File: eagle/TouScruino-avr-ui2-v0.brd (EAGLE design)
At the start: 63.5 x 72.4 mm, 60 parts, among them J1 AVR_ISP, Q1 8MHz, Q2 MMBT2222A, Q3 8MHz, U1 ATMEGA1284P, U2 AR1021, U3 MIC5209-3.3YS, U4 MCP73831, X2 USB

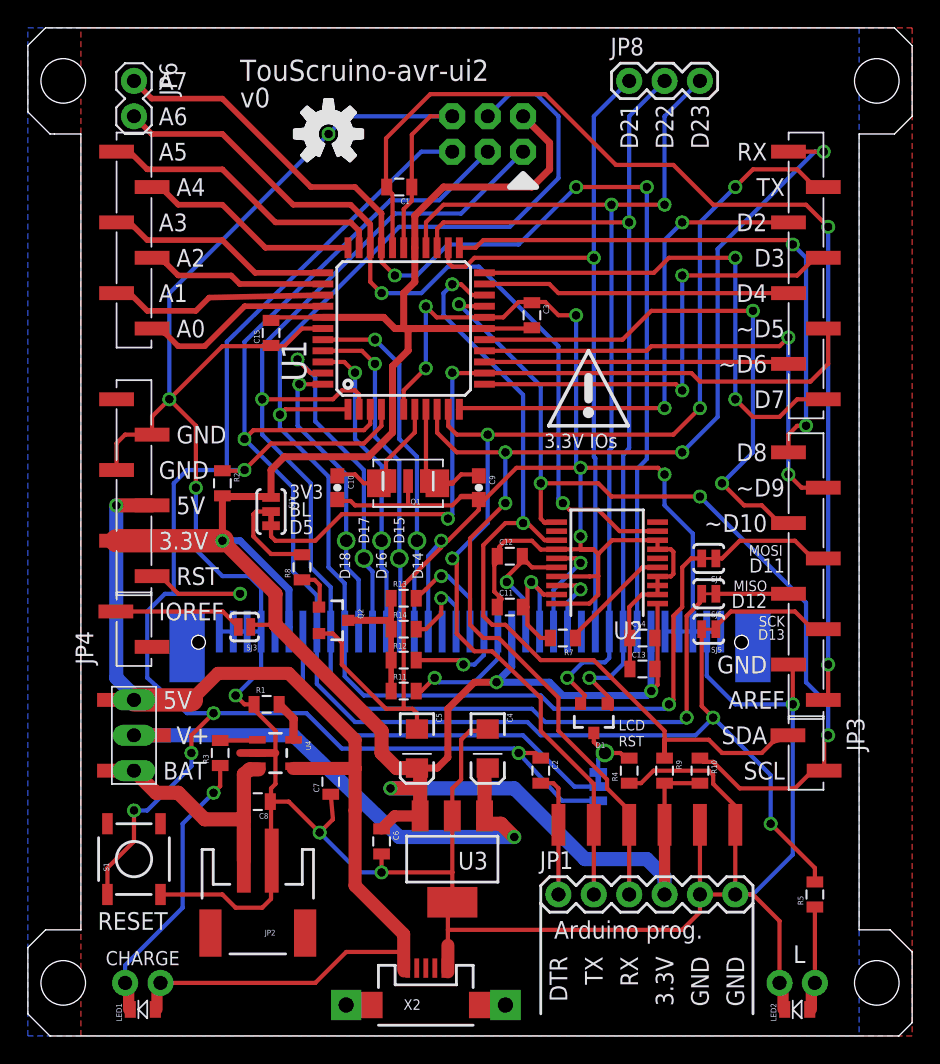
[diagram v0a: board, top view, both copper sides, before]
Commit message: 
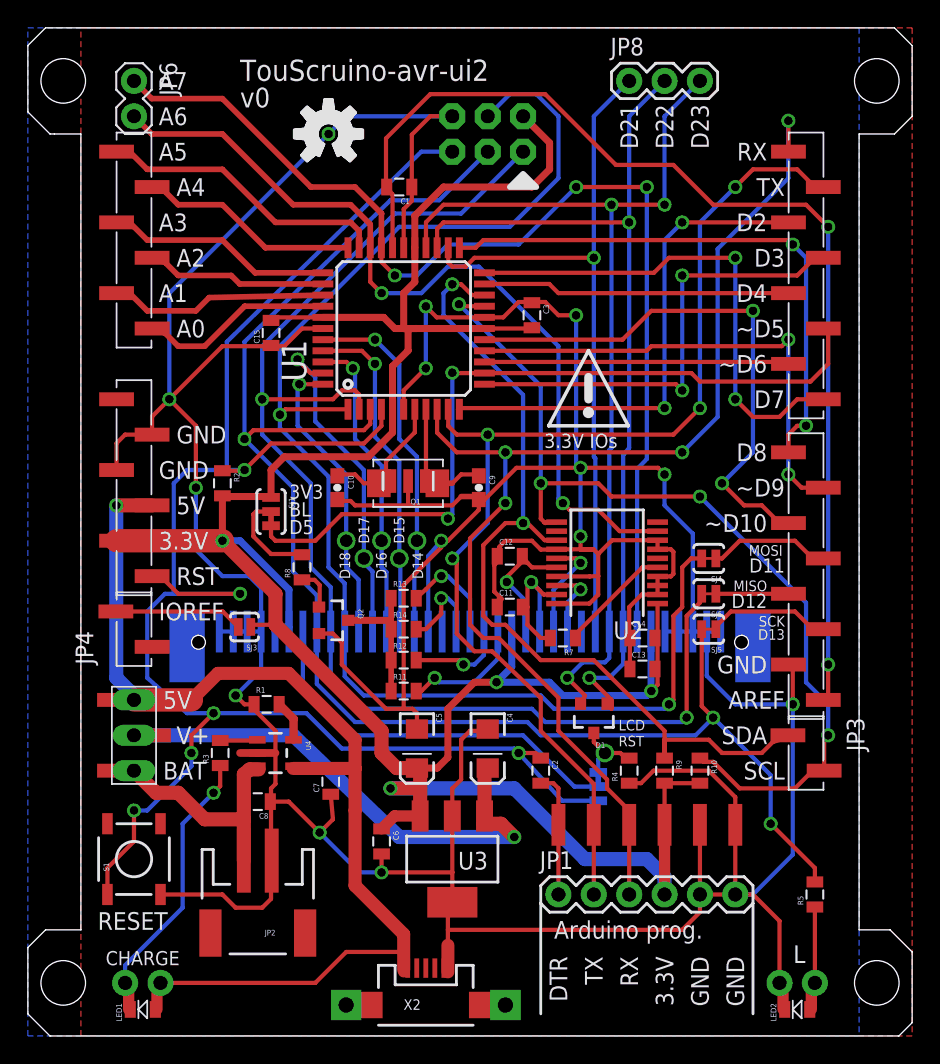
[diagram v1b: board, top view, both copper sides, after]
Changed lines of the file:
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@@
 <setting verticaltext="up"/>
 </settings>
-<grid distance="12.5" unitdist="mil" unit="mm" style="lines" multiple="8" display="yes" altdistance="6.25" altunitdist="mil" altunit="mil"/>
+<grid distance="12.5" unitdist="mil" unit="mil" style="lines" multiple="8" display="yes" altdistance="6.25" altunitdist="mil" altunit="mil"/>
 <layers>
 <layer number="1" name="Top" color="4" fill="1" visible="yes" active="yes"/>
@@
 <layer number="49" name="Reference" color="7" fill="1" visible="no" active="yes"/>
 <layer number="50" name="dxf" color="7" fill="1" visible="no" active="yes"/>
-<layer number="51" name="tDocu" color="14" fill="1" visible="no" active="yes"/>
+<layer number="51" name="tDocu" color="14" fill="1" visible="yes" active="yes"/>
 <layer number="52" name="bDocu" color="14" fill="1" visible="no" active="yes"/>
 <layer number="53" name="tGND_GNDA" color="7" fill="9" visible="no" active="no"/>
@@
 <wire x1="44.02625" y1="18.15" x2="44.92625" y2="19.05" width="0.3048" layer="1"/>
 <wire x1="44.92625" y1="19.05" x2="48.895" y2="19.05" width="0.3048" layer="1"/>
-<wire x1="48.895" y1="19.05" x2="49.2125" y2="18.7325" width="0.3048" layer="1"/>
-<wire x1="49.2125" y1="18.7325" x2="49.2125" y2="18.0975" width="0.3048" layer="1"/>
 <wire x1="52.07" y1="10.16" x2="50.8" y2="10.16" width="0.3048" layer="1"/>
 <wire x1="17.41" y1="16.8275" x2="17.41" y2="16.4575" width="0.3048" layer="1"/>
@@
 <wire x1="48.26" y1="15.16" x2="48.26" y2="10.16" width="0.3048" layer="1"/>
 <wire x1="50.8" y1="15.16" x2="50.8" y2="10.16" width="0.3048" layer="1"/>
-<wire x1="49.2125" y1="18.0975" x2="50.8" y2="16.51" width="0.3048" layer="1"/>
-<wire x1="50.8" y1="16.51" x2="50.8" y2="15.16" width="0.3048" layer="1"/>
+<wire x1="48.895" y1="19.05" x2="50.8" y2="17.145" width="0.3048" layer="1"/>
+<wire x1="50.8" y1="17.145" x2="50.8" y2="15.16" width="0.3048" layer="1"/>
 <wire x1="45.2175" y1="34.9475" x2="46.17375" y2="34.9475" width="0.3048" layer="1"/>
 <wire x1="46.355" y1="34.76625" x2="46.17375" y2="34.9475" width="0.3048" layer="1"/>
@@
 <wire x1="46.99" y1="41.91" x2="49.53" y2="44.45" width="0.3048" layer="16"/>
 <wire x1="49.53" y1="44.45" x2="49.53" y2="56.515" width="0.3048" layer="16"/>
-<wire x1="49.53" y1="56.515" x2="56.515" y2="63.5" width="0.3048" layer="16"/>
-<wire x1="56.515" y1="63.5" x2="57.15" y2="63.5" width="0.3048" layer="16"/>
-<wire x1="57.15" y1="63.5" x2="54.62" y2="63.5" width="0.3048" layer="1"/>
+<wire x1="49.53" y1="56.515" x2="54.61" y2="61.595" width="0.3048" layer="16"/>
+<wire x1="54.61" y1="61.595" x2="54.61" y2="65.7225" width="0.3048" layer="16"/>
+<wire x1="54.61" y1="65.7225" x2="54.62" y2="63.5" width="0.3048" layer="1"/>
 <wire x1="54.61" y1="63.5" x2="54.62" y2="63.5" width="0.3048" layer="1"/>
 <via x="46.99" y="41.91" extent="1-16" drill="0.6096"/>
-<via x="57.15" y="63.5" extent="1-16" drill="0.6096"/>
+<via x="54.61" y="65.7225" extent="1-16" drill="0.6096"/>
 <contactref element="JP9" pad="3"/>
 <wire x1="43.18" y1="10.16" x2="43.18" y2="15.16" width="0.3048" layer="1"/>
@@
 <contactref element="CN1" pad="25"/>
 <wire x1="25.4325" y1="40.925" x2="23.495" y2="42.8625" width="0.3048" layer="16"/>
-<wire x1="21.1875" y1="48.4" x2="22.72" y2="48.4" width="0.3048" layer="1"/>
-<wire x1="22.72" y1="48.4" x2="23.495" y2="47.625" width="0.3048" layer="1"/>
-<via x="23.495" y="47.625" extent="1-16" drill="0.6096"/>
-<wire x1="23.495" y1="42.8625" x2="23.495" y2="47.625" width="0.3048" layer="16"/>
+<wire x1="21.1875" y1="48.4" x2="22.87875" y2="48.4" width="0.3048" layer="1"/>
+<wire x1="22.87875" y1="48.4" x2="23.33625" y2="47.9425" width="0.3048" layer="1"/>
+<via x="23.33625" y="47.9425" extent="1-16" drill="0.6096"/>
+<wire x1="23.495" y1="42.8625" x2="23.495" y2="47.78375" width="0.3048" layer="16"/>
+<wire x1="23.495" y1="47.78375" x2="23.33625" y2="47.9425" width="0.3048" layer="16"/>
 <wire x1="25.75" y1="29.04" x2="25.75" y2="33.305" width="0.3048" layer="16"/>
 <wire x1="25.75" y1="33.305" x2="25.4" y2="33.655" width="0.3048" layer="16"/>
@@
 <wire x1="43.1675" y1="49.2" x2="44.4375" y2="49.2" width="0.3048" layer="1"/>
 <wire x1="44.4375" y1="49.2" x2="44.7675" y2="49.53" width="0.3048" layer="1"/>
-<wire x1="44.7675" y1="49.53" x2="53.975" y2="49.53" width="0.3048" layer="1"/>
-<wire x1="53.975" y1="49.53" x2="54.61" y2="50.165" width="0.3048" layer="1"/>
-<wire x1="54.61" y1="50.165" x2="54.61" y2="40.3225" width="0.3048" layer="16"/>
+<wire x1="44.7675" y1="49.53" x2="54.13375" y2="49.53" width="0.3048" layer="1"/>
+<wire x1="54.13375" y1="49.53" x2="54.61" y2="50.00625" width="0.3048" layer="1"/>
+<wire x1="54.61" y1="50.00625" x2="54.61" y2="40.3225" width="0.3048" layer="16"/>
 <wire x1="54.61" y1="40.3225" x2="55.5625" y2="39.37" width="0.3048" layer="1"/>
 <wire x1="55.5625" y1="39.37" x2="57.12" y2="39.37" width="0.3048" layer="1"/>
-<via x="54.61" y="50.165" extent="1-16" drill="0.6096"/>
+<via x="54.61" y="50.00625" extent="1-16" drill="0.6096"/>
 <via x="54.61" y="40.3225" extent="1-16" drill="0.6096"/>
 </signal>

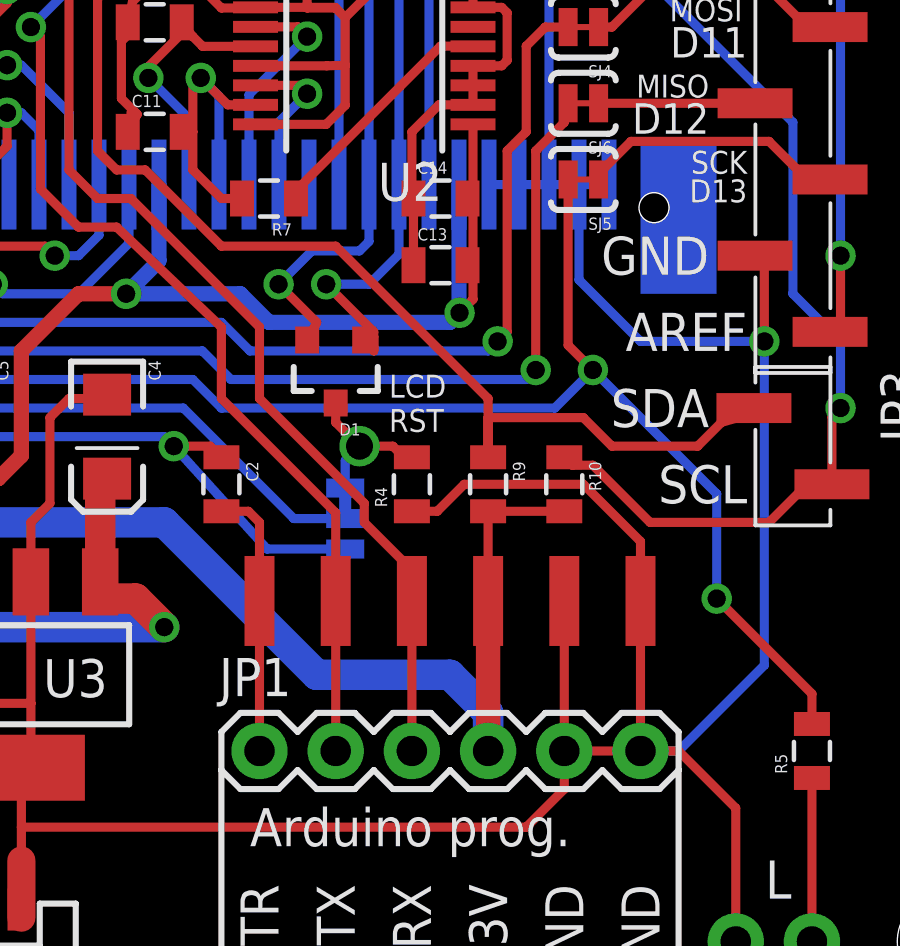
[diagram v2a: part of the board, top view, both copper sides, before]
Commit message: 
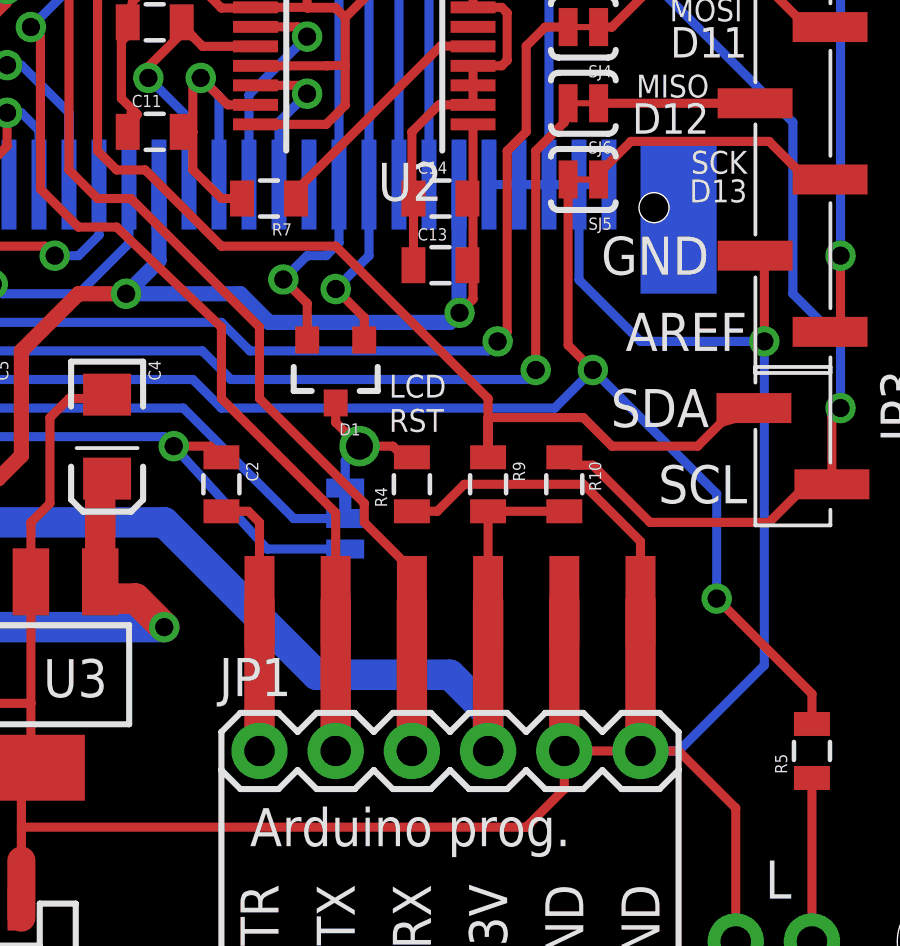
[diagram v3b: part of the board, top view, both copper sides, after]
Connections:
- net D21: now also D1.2
- net D22: no longer D1.1
- net D23: now also D1.1; no longer D1.2
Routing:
- net D22: track 65.0 -> 56.1 mm, vias 2 -> 1
- net D21: track 52.5 -> 59.2 mm, vias 1 -> 2
- net D23: track 68.1 -> 66.2 mm
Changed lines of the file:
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@@
 <layer number="27" name="tValues" color="7" fill="1" visible="no" active="yes"/>
 <layer number="28" name="bValues" color="7" fill="1" visible="no" active="yes"/>
-<layer number="29" name="tStop" color="7" fill="3" visible="yes" active="yes"/>
+<layer number="29" name="tStop" color="7" fill="3" visible="no" active="yes"/>
 <layer number="30" name="bStop" color="7" fill="6" visible="no" active="yes"/>
 <layer number="31" name="tCream" color="7" fill="4" visible="no" active="yes"/>
@@
 <wire x1="47.75" y1="36.07" x2="45.72" y2="38.1" width="0.3048" layer="16"/>
 <wire x1="45.72" y1="38.1" x2="45.72" y2="40.3225" width="0.3048" layer="16"/>
-<wire x1="48.26" y1="15.16" x2="48.26" y2="10.16" width="0.3048" layer="1"/>
-<wire x1="50.8" y1="15.16" x2="50.8" y2="10.16" width="0.3048" layer="1"/>
+<wire x1="48.26" y1="15.16" x2="48.26" y2="10.16" width="1.016" layer="1"/>
+<wire x1="50.8" y1="15.16" x2="50.8" y2="10.16" width="1.016" layer="1"/>
 <wire x1="48.895" y1="19.05" x2="50.8" y2="17.145" width="0.3048" layer="1"/>
 <wire x1="50.8" y1="17.145" x2="50.8" y2="15.16" width="0.3048" layer="1"/>
@@
 <contactref element="JP1" pad="1"/>
 <contactref element="JP9" pad="1"/>
-<wire x1="38.1" y1="10.16" x2="38.1" y2="15.16" width="0.3048" layer="1"/>
+<wire x1="38.1" y1="10.16" x2="38.1" y2="15.16" width="1.016" layer="1"/>
 <wire x1="36.83" y1="18.15" x2="37.73" y2="18.15" width="0.3048" layer="1"/>
 <wire x1="37.73" y1="18.15" x2="38.1" y2="17.78" width="0.3048" layer="1"/>
@@
 <wire x1="26.035" y1="17.78" x2="28.1686" y2="17.78" width="1.016" layer="1"/>
 <contactref element="JP9" pad="4"/>
-<wire x1="45.72" y1="10.16" x2="45.72" y2="15.16" width="0.8128" layer="1"/>
+<wire x1="45.72" y1="10.16" x2="45.72" y2="15.16" width="1.016" layer="1"/>
 <wire x1="45.72" y1="15.16" x2="45.72" y2="18.15" width="0.3048" layer="1"/>
 </signal>
@@
 <via x="54.61" y="65.7225" extent="1-16" drill="0.6096"/>
 <contactref element="JP9" pad="3"/>
-<wire x1="43.18" y1="10.16" x2="43.18" y2="15.16" width="0.3048" layer="1"/>
+<wire x1="43.18" y1="10.16" x2="43.18" y2="15.16" width="1.016" layer="1"/>
 <wire x1="41.5925" y1="17.78" x2="43.18" y2="16.1925" width="0.3048" layer="1"/>
 <wire x1="43.18" y1="16.1925" x2="43.18" y2="15.16" width="0.3048" layer="1"/>
@@
 <via x="50.8" y="60.96" extent="1-16" drill="0.6096"/>
 <contactref element="JP9" pad="2"/>
-<wire x1="40.64" y1="10.16" x2="40.64" y2="15.16" width="0.3048" layer="1"/>
+<wire x1="40.64" y1="10.16" x2="40.64" y2="15.16" width="1.016" layer="1"/>
 </signal>
 <signal name="N$5">
@@
 <signal name="D23">
 <contactref element="U1" pad="26"/>
-<contactref element="D1" pad="2"/>
 <contactref element="CN1" pad="9"/>
 <wire x1="41.75" y1="29.04" x2="41.75" y2="42.07" width="0.3048" layer="16"/>
 <wire x1="41.75" y1="42.07" x2="41.91" y2="42.2275" width="0.3048" layer="16"/>
-<wire x1="41.75" y1="29.04" x2="41.75" y2="27.145" width="0.3048" layer="16"/>
-<wire x1="41.75" y1="27.145" x2="41.43375" y2="26.82875" width="0.3048" layer="16"/>
-<wire x1="41.43375" y1="26.82875" x2="39.84625" y2="26.82875" width="0.3048" layer="16"/>
-<wire x1="39.84625" y1="26.82875" x2="38.735" y2="25.7175" width="0.3048" layer="16"/>
-<via x="38.735" y="25.7175" extent="1-16" drill="0.6096"/>
-<wire x1="39.69" y1="23.86" x2="40.0075" y2="24.445" width="0.3048" layer="1"/>
-<wire x1="40.0075" y1="24.445" x2="38.735" y2="25.7175" width="0.3048" layer="1"/>
 <wire x1="41.91" y1="42.2275" x2="41.91" y2="59.69" width="0.3048" layer="16"/>
 <wire x1="28.5875" y1="56.6" x2="28.5875" y2="58.4325" width="0.3048" layer="1"/>
@@
 <wire x1="45.72" y1="66.04" x2="48.26" y2="68.58" width="0.3048" layer="16"/>
 <via x="45.72" y="59.69" extent="1-16" drill="0.6096"/>
+<contactref element="D1" pad="1"/>
+<wire x1="41.75" y1="29.04" x2="41.75" y2="26.66875" width="0.3048" layer="16"/>
+<wire x1="41.75" y1="26.66875" x2="40.64" y2="25.55875" width="0.3048" layer="16"/>
+<wire x1="40.64" y1="25.55875" x2="41.5925" y2="24.60625" width="0.3048" layer="1"/>
+<via x="40.64" y="25.55875" extent="1-16" drill="0.6096"/>
+<wire x1="41.5925" y1="24.60625" x2="41.5925" y2="23.8625" width="0.3048" layer="1"/>
+<wire x1="41.5925" y1="23.8625" x2="41.59" y2="23.86" width="0.3048" layer="1"/>
 </signal>
 <signal name="D22">
 <contactref element="U1" pad="25"/>
-<contactref element="D1" pad="1"/>
 <contactref element="CN1" pad="8"/>
 <wire x1="42.75" y1="29.04" x2="42.75" y2="41.705" width="0.3048" layer="16"/>
 <wire x1="42.75" y1="41.705" x2="43.18" y2="42.2275" width="0.3048" layer="16"/>
-<via x="40.3225" y="25.7175" extent="1-16" drill="0.6096"/>
-<wire x1="42.75" y1="29.04" x2="42.75" y2="26.71625" width="0.3048" layer="16"/>
-<wire x1="42.75" y1="26.71625" x2="41.75125" y2="25.7175" width="0.3048" layer="16"/>
-<wire x1="41.75125" y1="25.7175" x2="40.3225" y2="25.7175" width="0.3048" layer="16"/>
-<wire x1="41.59" y1="23.86" x2="41.9075" y2="23.97375" width="0.3048" layer="1"/>
-<wire x1="41.9075" y1="23.97375" x2="41.91" y2="23.495" width="0.3048" layer="1"/>
-<wire x1="41.91" y1="23.495" x2="41.91" y2="24.13" width="0.3048" layer="1"/>
-<wire x1="41.91" y1="24.13" x2="40.3225" y2="25.7175" width="0.3048" layer="1"/>
 <wire x1="43.18" y1="42.2275" x2="43.18" y2="58.42" width="0.3048" layer="16"/>
 <wire x1="29.3875" y1="56.6" x2="29.3875" y2="57.9625" width="0.3048" layer="1"/>
@@
 <wire x1="40.64" y1="55.88" x2="40.64" y2="66.04" width="0.3048" layer="16"/>
 <wire x1="40.64" y1="66.04" x2="43.18" y2="68.58" width="0.3048" layer="16"/>
+<contactref element="D1" pad="2"/>
+<wire x1="40.75" y1="29.04" x2="40.75" y2="27.0975" width="0.3048" layer="16"/>
+<wire x1="40.75" y1="27.0975" x2="40.3225" y2="26.67" width="0.3048" layer="16"/>
+<wire x1="40.3225" y1="26.67" x2="39.6875" y2="26.67" width="0.3048" layer="16"/>
+<wire x1="39.6875" y1="26.67" x2="38.89375" y2="25.87625" width="0.3048" layer="16"/>
+<wire x1="39.69" y1="23.86" x2="39.69" y2="25.08" width="0.3048" layer="1"/>
+<wire x1="39.69" y1="25.08" x2="38.89375" y2="25.87625" width="0.3048" layer="1"/>
+<via x="38.89375" y="25.87625" extent="1-16" drill="0.6096"/>
 </signal>
 <signal name="N$9">
@@
 </signal>
 </signals>
-<errors>
-</errors>
 </board>
 </drawing>
